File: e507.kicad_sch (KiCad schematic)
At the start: 15 parts, among them J1 Micro_SD_Card, SW1 TS-1088-AR02016, SW2 TS-1088-AR02016, U1 BQ25185DLHR, U2 ESP32-S3-WROOM-1

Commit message: all part symbols downloaded
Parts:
- U2: footprint RF_Module:ESP32-S3-WROOM-1U -> PCM_Espressif:ESP32-S3-WROOM-1
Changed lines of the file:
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@@
 	)
 	(no_connect
-		(at 114.3 52.07)
+		(at 90.17 52.07)
 	)
 	(no_connect
-		(at 114.3 95.25)
+		(at 90.17 95.25)
 	)
 	(no_connect
@@
 	)
 	(no_connect
-		(at 114.3 92.71)
+		(at 90.17 92.71)
 	)
 	(wire
@@
 	)
 	(label "USB_DN"
-		(at 114.3 39.37 0)
+		(at 90.17 39.37 0)
 		(effects
 			(font
@@
 	)
 	(label "USB_DP"
-		(at 114.3 36.83 0)
+		(at 90.17 36.83 0)
 		(effects
 			(font
@@
 	(global_label "BOOT"
 		(shape input)
-		(at 114.3 44.45 0)
+		(at 90.17 44.45 0)
 		(fields_autoplaced yes)
 		(effects
@@
 		)
 		(property "Intersheetrefs" "${INTERSHEET_REFS}"
-			(at 122.1838 44.45 0)
+			(at 98.0538 44.45 0)
 			(hide yes)
 			(show_name no)
@@
 	(global_label "RESET"
 		(shape input)
-		(at 22.86 29.21 180)
+		(at 46.99 29.21 180)
 		(fields_autoplaced yes)
 		(effects
@@
 		)
 		(property "Intersheetrefs" "${INTERSHEET_REFS}"
-			(at 14.1297 29.21 0)
+			(at 38.2597 29.21 0)
 			(hide yes)
 			(show_name no)
@@
 	)
 	(symbol
+		(lib_id "Espressif:ESP32-S3-WROOM-1")
+		(at 68.58 64.77 0)
+		(unit 1)
+		(body_style 1)
+		(exclude_from_sim no)
+		(in_bom yes)
+		(on_board yes)
+		(in_pos_files yes)
+		(dnp no)
+		(fields_autoplaced yes)
+		(property "Reference" "U2"
+			(at 70.7233 21.59 0)
+			(show_name no)
+			(do_not_autoplace no)
+			(effects
+				(font
+					(size 1.27 1.27)
+				)
+				(justify left)
+			)
+		)
+		(property "Value" "ESP32-S3-WROOM-1"
+			(at 70.7233 24.13 0)
+			(show_name no)
+			(do_not_autoplace no)
+			(effects
+				(font
+					(size 1.27 1.27)
+				)
+				(justify left)
+			)
+		)
+		(property "Footprint" "PCM_Espressif:ESP32-S3-WROOM-1"
+			(at 71.12 113.03 0)
+			(hide yes)
+			(show_name no)
+			(do_not_autoplace no)
+			(effects
+				(font
+					(size 1.27 1.27)
+				)
+			)
+		)
+		(property "Datasheet" "https://www.espressif.com/sites/default/files/documentation/esp32-s3-wroom-1_wroom-1u_datasheet_en.pdf"
+			(at 71.12 115.57 0)
+			(hide yes)
+			(show_name no)
+			(do_not_autoplace no)
+			(effects
+				(font
+					(size 1.27 1.27)
+				)
+			)
+		)
+		(property "Description" "2.4 GHz WiFi (802.11 b/g/n) and Bluetooth ® 5 (LE) module Built around ESP32S3 series of SoCs, Xtensa ® dualcore 32bit LX7 microprocessor Flash up to 16 MB, PSRAM up to 8 MB 36 GPIOs, rich set of peripherals Onboard PCB antenna"
+			(at 68.58 64.77 0)
+			(hide yes)
+			(show_name no)
+			(do_not_autoplace no)
+			(effects
+				(font
+					(size 1.27 1.27)
+				)
+			)
+		)
+		(pin "12"
+		)
+		(pin "11"
+		)
+		(pin "10"
+		)
+		(pin "9"
+		)
+		(pin "8"
+		)
+		(pin "7"
+		)
+		(pin "5"
+		)
+		(pin "4"
+		)
+		(pin "1"
+		)
+		(pin "6"
+		)
+		(pin "3"
+		)
+		(pin "2"
+		)
+		(pin "13"
+		)
+		(pin "41"
+		)
+		(pin "21"
+		)
+		(pin "26"
+		)
+		(pin "25"
+		)
+		(pin "16"
+		)
+		(pin "24"
+		)
+		(pin "28"
+		)
+		(pin "27"
+		)
+		(pin "22"
+		)
+		(pin "17"
+		)
+		(pin "30"
+		)
+		(pin "23"
+		)
+		(pin "18"
+		)
+		(pin "14"
+		)
+		(pin "20"
+		)
+		(pin "31"
+		)
+		(pin "32"
+		)
+		(pin "33"
+		)
+		(pin "19"
+		)
+		(pin "15"
+		)
+		(pin "29"
+		)
+		(pin "35"
+		)
+		(pin "34"
+		)
+		(pin "37"
+		)
+		(pin "36"
+		)
+		(pin "38"
+		)
+		(pin "40"
+		)
+		(pin "39"
+		)
+		(instances
+			(project "e507"
+				(path "/acf7fdfc-08c7-4b01-88b5-5cee2f49d989"
+					(reference "U2")
+					(unit 1)
+				)
+			)
+		)
+	)
+	(symbol
 		(lib_id "Device:R_Small")
 		(at 180.34 40.64 0)
@@
 					(unit 1)
 				)
-			)
-		)
-	)
-	(symbol
-		(lib_id "Espressif:ESP32-S3-WROOM-1")
-		(at 68.58 64.77 0)
-		(unit 1)
-		(body_style 1)
-		(exclude_from_sim no)
-		(in_bom yes)
-		(on_board yes)
-		(in_pos_files yes)
-		(dnp no)
-		(fields_autoplaced yes)
-		(property "Reference" "U2"
-			(at 70.7233 21.59 0)
-			(show_name no)
-			(do_not_autoplace no)
-			(effects
-				(font
-					(size 1.27 1.27)
-				)
-				(justify left)
-			)
-		)
-		(property "Value" "ESP32-S3-WROOM-1"
-			(at 70.7233 24.13 0)
-			(show_name no)
-			(do_not_autoplace no)
-			(effects
-				(font
-					(size 1.27 1.27)
-				)
-				(justify left)
-			)
-		)
-		(property "Footprint" "RF_Module:ESP32-S3-WROOM-1U"
-			(at 71.12 113.03 0)
-			(hide yes)
-			(show_name no)
-			(do_not_autoplace no)
-			(effects
-				(font
-					(size 1.27 1.27)
-				)
-			)
-		)
-		(property "Datasheet" "https://www.espressif.com/sites/default/files/documentation/esp32-s3-wroom-1_wroom-1u_datasheet_en.pdf"
-			(at 71.12 115.57 0)
-			(hide yes)
-			(show_name no)
-			(do_not_autoplace no)
-			(effects
-				(font
-					(size 1.27 1.27)
-				)
-			)
-		)
-		(property "Description" "2.4 GHz WiFi (802.11 b/g/n) and Bluetooth ® 5 (LE) module Built around ESP32S3 series of SoCs, Xtensa ® dualcore 32bit LX7 microprocessor Flash up to 16 MB, PSRAM up to 8 MB 36 GPIOs, rich set of peripherals Onboard PCB antenna"
-			(at 68.58 64.77 0)
-			(hide yes)
-			(show_name no)
-			(do_not_autoplace no)
-			(effects
-				(font
-					(size 1.27 1.27)
-				)
-			)
-		)
-		(pin "22"
-		)
-		(pin "37"
-		)
-		(pin "29"
-		)
-		(pin "30"
-		)
-		(pin "27"
-		)
-		(pin "1"
-		)
-		(pin "38"
-		)
-		(pin "26"
-		)
-		(pin "31"
-		)
-		(pin "41"
-		)
-		(pin "23"
-		)
-		(pin "40"
-		)
-		(pin "2"
-		)
-		(pin "20"
-		)
-		(pin "36"
-		)
-		(pin "28"
-		)
-		(pin "33"
-		)
-		(pin "32"
-		)
-		(pin "35"
-		)
-		(pin "34"
-		)
-		(pin "18"
-		)
-		(pin "3"
-		)
-		(pin "4"
-		)
-		(pin "5"
-		)
-		(pin "6"
-		)
-		(pin "7"
-		)
-		(pin "8"
-		)
-		(pin "9"
-		)
-		(pin "10"
-		)
-		(pin "11"
-		)
-		(pin "12"
-		)
-		(pin "13"
-		)
-		(pin "14"
-		)
-		(pin "15"
-		)
-		(pin "16"
-		)
-		(pin "25"
-		)
-		(pin "24"
-		)
-		(pin "17"
-		)
-		(pin "19"
-		)
-		(pin "21"
-		)
-		(pin "39"
-		)
-		(instances
-			(project "e507"
-				(path "/acf7fdfc-08c7-4b01-88b5-5cee2f49d989"
-					(reference "U2")
-					(unit 1)
-				)

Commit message: import symbols
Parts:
- removed C1, C2: 1uF, symbol Device:C
- removed C3, C4: 1uF, Package_SON:WSON-6-1EP_3x3mm_P0.95mm, symbol Device:C
- removed D1: SS34, Diode_SMD:D_SMA, symbol Diode:SS34
- removed J1: Micro_SD_Card, Diode_SMD:D_SMA, symbol Connector:Micro_SD_Card
- removed R1, R2: 10K, SW_TS-1088_XNP, symbol Device:R
- removed R3, R4: 5.1K, Resistor_THT:R_Array_SIP4, symbol Device:R_Small
- removed SW1, SW2: TS-1088-AR02016, SW_TS-1088_XNP, symbol buttons:TS-1088-AR02016
- removed U1: BQ25185DLHR, WSON10_DLH_TEX, symbol bq25185:BQ25185DLHR
- removed U2: ESP32-S3-WROOM-1, PCM_Espressif:ESP32-S3-WROOM-1, symbol Espressif:ESP32-S3-WROOM-1
- removed USB1: 12402012E212A, 12402012E212A:AMPHENOL_12402012E212A, symbol 12402012E212A:12402012E212A
- added S1: TS-1088-AR02016, flat-button:SW_TS-1088-AR02016, symbol TS-1088-AR02016:TS-1088-AR02016
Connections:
- no-connect marks 5 -> 0
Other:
- note removed: "Dev Buttons"

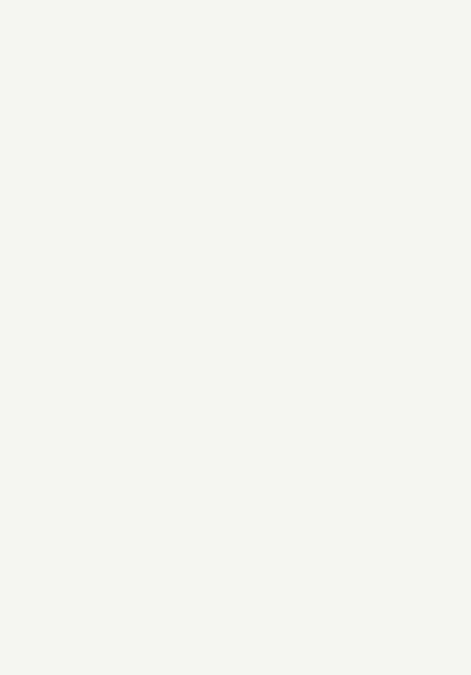
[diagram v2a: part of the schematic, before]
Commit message: start power schematic
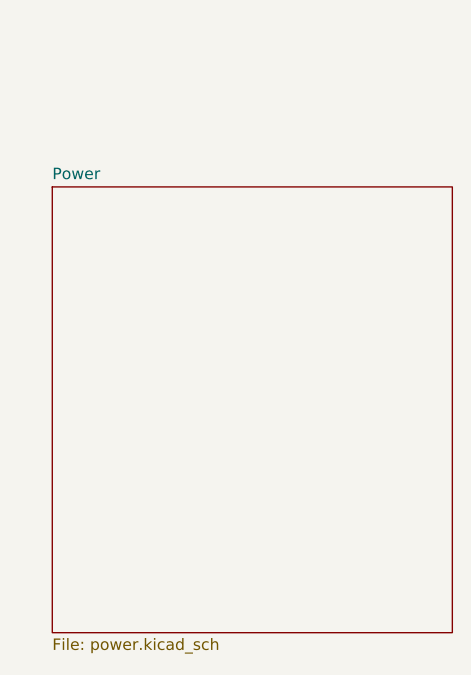
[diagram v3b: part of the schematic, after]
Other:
- added sheet Power (power.kicad_sch)
- title: (none) -> MP3 Player
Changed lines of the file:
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@@
 	(generator_version "10.0")
 	(paper "A4")
+	(title_block
+		(title "MP3 Player")
+	)
 	(symbol
 		(lib_id "TS-1088-AR02016:TS-1088-AR02016")
@@
 				)
 			)
+		)
+	)
+	(sheet
+		(at 33.02 99.695)
+		(size 44.45 49.53)
+		(exclude_from_sim no)
+		(in_bom yes)
+		(on_board yes)
+		(dnp no)
+		(fields_autoplaced yes)
+		(stroke
+			(width 0.1524)
+			(type solid)
+		)
+		(fill
+			(color 0 0 0 0)
+		)
+		(property "Sheetname" "Power"
+			(at 33.02 98.9834 0)
+			(show_name no)
+			(do_not_autoplace no)
+			(effects
+				(font
+					(size 1.27 1.27)
+				)
+				(justify left bottom)
+			)
+		)
+		(property "Sheetfile" "power.kicad_sch"
+			(at 33.02 149.8096 0)
+			(show_name no)
+			(do_not_autoplace no)
+			(effects
+				(font
+					(size 1.27 1.27)
+				)
+				(justify left top)
+			)
+		)
+		(instances
+			(project "e507"
+				(path "/acf7fdfc-08c7-4b01-88b5-5cee2f49d989"
+					(page "2")
+				)
+			)

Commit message: mcu & audio
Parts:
- removed S1: TS-1088-AR02016, flat-button:SW_TS-1088-AR02016, symbol TS-1088-AR02016:TS-1088-AR02016
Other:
- added sheet Audio (audio.kicad_sch)
- added sheet MCU (mcu.kicad_sch)
- sheet Power ports: added IO_AUDIO_EN, IO_BAT_V, IO_CHG_STAT1, IO_CHG_STAT2, USB_D+, USB_D-; removed none

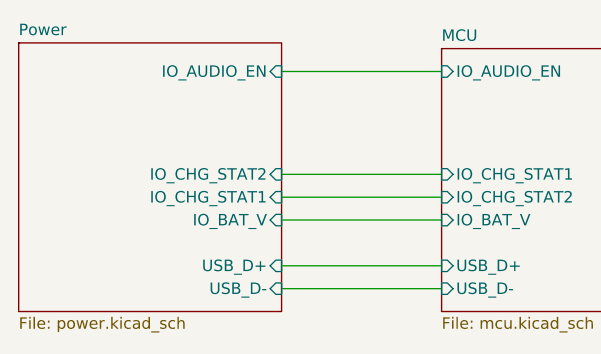
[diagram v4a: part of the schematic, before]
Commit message: add usb data esd
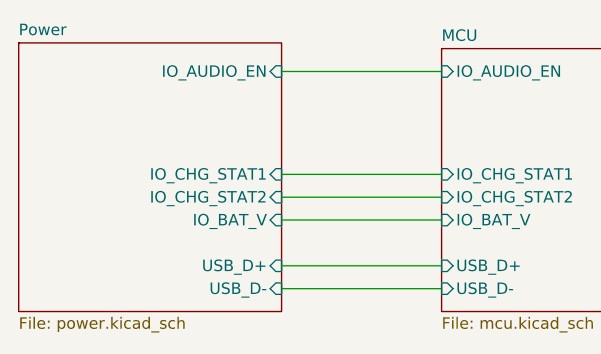
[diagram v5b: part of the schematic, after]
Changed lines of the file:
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@@
+	(wire
+		(pts
+			(xy 82.55 93.98) (xy 100.33 93.98)
+		)
+		(stroke
+			(width 0)
+			(type default)
+		)
+	)
+	(wire
+		(pts
+			(xy 82.55 82.55) (xy 100.33 82.55)
+		)
+		(stroke
+			(width 0)
+			(type default)
+		)
+	)
 	(wire
 		(pts
 			(xy 82.55 96.52) (xy 100.33 96.52)
-		)
-		(stroke
-			(width 0)
-			(type default)
-		)
-	)
-	(wire
-		(pts
-			(xy 82.55 93.98) (xy 100.33 93.98)
-		)
-		(stroke
-			(width 0)
-			(type default)
-		)
-	)
-	(wire
-		(pts
-			(xy 82.55 82.55) (xy 100.33 82.55)
 		)
 		(stroke
@@
 		)
 		(pin "IO_CHG_STAT1" input
+			(at 82.55 93.98 0)
+			(effects
+				(font
+					(size 1.27 1.27)
+				)
+				(justify right)
+			)
+		)
+		(pin "IO_CHG_STAT2" input
 			(at 82.55 96.52 0)
 			(effects
 				(font
-					(size 1.27 1.27)
-				)
-				(justify right)
-			)
-		)
-		(pin "IO_CHG_STAT2" input
-			(at 82.55 93.98 0)
-			(effects
-				(font

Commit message: work on pcb
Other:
- sheet Audio ports: added IO_DAC_BCK, IO_DAC_DIN, IO_DAC_LRCK; removed none
- sheet MCU ports: added IO_DAC_BCK, IO_DAC_DIN, IO_DAC_LRCK; removed none
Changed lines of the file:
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@@
+	(wire
+		(pts
+			(xy 135.89 90.17) (xy 153.67 90.17)
+		)
+		(stroke
+			(width 0)
+			(type default)
+		)
+	)
 	(wire
 		(pts
@@
 	(wire
 		(pts
+			(xy 135.89 95.25) (xy 153.67 95.25)
+		)
+		(stroke
+			(width 0)
+			(type default)
+		)
+	)
+	(wire
+		(pts
 			(xy 82.55 82.55) (xy 100.33 82.55)
 		)
@@
 		(pts
 			(xy 82.55 96.52) (xy 100.33 96.52)
+		)
+		(stroke
+			(width 0)
+			(type default)
+		)
+	)
+	(wire
+		(pts
+			(xy 135.89 92.71) (xy 153.67 92.71)
 		)
 		(stroke
@@
 			)
 		)
+		(pin "IO_DAC_BCK" input
+			(at 135.89 92.71 0)
+			(effects
+				(font
+					(size 1.27 1.27)
+				)
+				(justify right)
+			)
+		)
+		(pin "IO_DAC_DIN" input
+			(at 135.89 90.17 0)
+			(effects
+				(font
+					(size 1.27 1.27)
+				)
+				(justify right)
+			)
+		)
+		(pin "IO_DAC_LRCK" input
+			(at 135.89 95.25 0)
+			(effects
+				(font
+					(size 1.27 1.27)
+				)
+				(justify right)
+			)
+		)
 		(instances
 			(project "e507"
@@
 			)
 		)
+		(pin "IO_DAC_BCK" input
+			(at 153.67 92.71 180)
+			(effects
+				(font
+					(size 1.27 1.27)
+				)
+				(justify left)
+			)
+		)
+		(pin "IO_DAC_DIN" input
+			(at 153.67 90.17 180)
+			(effects
+				(font
+					(size 1.27 1.27)
+				)
+				(justify left)
+			)
+		)
+		(pin "IO_DAC_LRCK" input
+			(at 153.67 95.25 180)
+			(effects
+				(font
+					(size 1.27 1.27)
+				)
+				(justify left)
+			)
+		)

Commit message: fucker
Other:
- sheet Audio ports: added IO_AMP_EN, IO_DAC_SCK; removed none
- sheet MCU ports: added IO_DAC_SCK; removed none
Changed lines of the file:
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@@
 		(title "MP3 Player")
 	)
+	(junction
+		(at 96.52 82.55)
+		(diameter 0)
+		(color 0 0 0 0)
+	)
 	(wire
 		(pts
@@
 	(wire
 		(pts
-			(xy 135.89 90.17) (xy 153.67 90.17)
+			(xy 82.55 96.52) (xy 100.33 96.52)
+		)
+		(stroke
+			(width 0)
+			(type default)
+		)
+	)
+	(wire
+		(pts
+			(xy 146.05 76.2) (xy 146.05 82.55)
 		)
 		(stroke
@@
 	(wire
 		(pts
-			(xy 135.89 95.25) (xy 153.67 95.25)
-		)
-		(stroke
-			(width 0)
-			(type default)
-		)
-	)
-	(wire
-		(pts
-			(xy 82.55 82.55) (xy 100.33 82.55)
-		)
-		(stroke
-			(width 0)
-			(type default)
-		)
-	)
-	(wire
-		(pts
-			(xy 82.55 96.52) (xy 100.33 96.52)
-		)
-		(stroke
-			(width 0)
-			(type default)
-		)
-	)
-	(wire
-		(pts
-			(xy 135.89 92.71) (xy 153.67 92.71)
+			(xy 96.52 76.2) (xy 146.05 76.2)
+		)
+		(stroke
+			(width 0)
+			(type default)
+		)
+	)
+	(wire
+		(pts
+			(xy 96.52 82.55) (xy 96.52 76.2)
+		)
+		(stroke
+			(width 0)
+			(type default)
+		)
+	)
+	(wire
+		(pts
+			(xy 82.55 82.55) (xy 96.52 82.55)
+		)
+		(stroke
+			(width 0)
+			(type default)
+		)
+	)
+	(wire
+		(pts
+			(xy 96.52 82.55) (xy 100.33 82.55)
+		)
+		(stroke
+			(width 0)
+			(type default)
+		)
+	)
+	(wire
+		(pts
+			(xy 135.89 99.06) (xy 153.67 99.06)
 		)
 		(stroke
@@
 		(pts
 			(xy 82.55 104.14) (xy 100.33 104.14)
+		)
+		(stroke
+			(width 0)
+			(type default)
+		)
+	)
+	(wire
+		(pts
+			(xy 135.89 101.6) (xy 153.67 101.6)
+		)
+		(stroke
+			(width 0)
+			(type default)
+		)
+	)
+	(wire
+		(pts
+			(xy 135.89 106.68) (xy 153.67 106.68)
+		)
+		(stroke
+			(width 0)
+			(type default)
+		)
+	)
+	(wire
+		(pts
+			(xy 146.05 82.55) (xy 153.67 82.55)
+		)
+		(stroke
+			(width 0)
+			(type default)
+		)
+	)
+	(wire
+		(pts
+			(xy 135.89 104.14) (xy 153.67 104.14)
 		)
 		(stroke
@@
 		)
 		(pin "IO_DAC_BCK" input
-			(at 135.89 92.71 0)
+			(at 135.89 104.14 0)
 			(effects
 				(font
@@
 		)
 		(pin "IO_DAC_DIN" input
-			(at 135.89 90.17 0)
+			(at 135.89 101.6 0)
 			(effects
 				(font
@@
 		)
 		(pin "IO_DAC_LRCK" input
-			(at 135.89 95.25 0)
+			(at 135.89 106.68 0)
+			(effects
+				(font
+					(size 1.27 1.27)
+				)
+				(justify right)
+			)
+		)
+		(pin "IO_DAC_SCK" input
+			(at 135.89 99.06 0)
 			(effects
 				(font
@@
 		)
 		(pin "IO_CHG_STAT1" input
+			(at 82.55 96.52 0)
+			(effects
+				(font
+					(size 1.27 1.27)
+				)
+				(justify right)
+			)
+		)
+		(pin "IO_CHG_STAT2" input
 			(at 82.55 93.98 0)
-			(effects
-				(font
-					(size 1.27 1.27)
-				)
-				(justify right)
-			)
-		)
-		(pin "IO_CHG_STAT2" input
-			(at 82.55 96.52 0)
 			(effects
 				(font
@@
 			)
 		)
+		(pin "IO_AMP_EN" input
+			(at 153.67 82.55 180)
+			(effects
+				(font
+					(size 1.27 1.27)
+				)
+				(justify left)
+			)
+		)
 		(pin "IO_DAC_BCK" input
-			(at 153.67 92.71 180)
+			(at 153.67 104.14 180)
 			(effects
 				(font
@@
 		)
 		(pin "IO_DAC_DIN" input
-			(at 153.67 90.17 180)
+			(at 153.67 101.6 180)
 			(effects
 				(font
@@
 		)
 		(pin "IO_DAC_LRCK" input
-			(at 153.67 95.25 180)
-			(effects
-				(font
+			(at 153.67 106.68 180)
+			(effects
+				(font
+					(size 1.27 1.27)
+				)
+				(justify left)
+			)
+		)
+		(pin "IO_DAC_SCK" input
+			(at 153.67 99.06 180)
+			(effects
+				(font

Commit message: Finish? schematic
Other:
- sheet Audio ports: added none; removed IO_DAC_SCK
- sheet MCU ports: added none; removed IO_DAC_SCK
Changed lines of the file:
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@@
-	(wire
-		(pts
-			(xy 135.89 99.06) (xy 153.67 99.06)
-		)
-		(stroke
-			(width 0)
-			(type default)
-		)
-	)
 	(wire
 		(pts
@@
 			)
 		)
-		(pin "IO_DAC_SCK" input
-			(at 135.89 99.06 0)
-			(effects
-				(font
-					(size 1.27 1.27)
-				)
-				(justify right)
-			)
-		)
 		(instances
 			(project "e507"
@@
 			(effects
 				(font
-					(size 1.27 1.27)
-				)
-				(justify left)
-			)
-		)
-		(pin "IO_DAC_SCK" input
-			(at 153.67 99.06 180)
-			(effects
-				(font
